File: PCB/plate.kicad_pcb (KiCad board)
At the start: 2 copper layers, 354 x 121 mm, 126 parts, among them SW10 EC_SW, SW11 EC_SW, SW12 EC_SW, SW13 EC_SW, SW14 EC_SW, SW15 EC_SW, SW16 EC_SW, SW17 EC_SW, SW18 EC_SW, SW19 EC_SW, SW2 EC_SW, SW20 EC_SW, SW21 EC_SW, SW22 EC_SW, SW23 EC_SW, SW24 EC_SW, SW25 EC_SW, SW26 EC_SW, SW27 EC_SW, SW28 EC_SW, SW29 EC_SW, SW3 EC_SW, SW30 EC_SW, SW31 EC_SW, SW32 EC_SW, SW33 EC_SW, SW34 EC_SW, SW35 EC_SW, SW36 EC_SW, SW37 EC_SW, SW38 EC_SW, SW39 EC_SW, SW4 EC_SW, SW40 EC_SW, SW41 EC_SW, SW42 EC_SW, SW43 EC_SW, SW44 EC_SW, SW45 EC_SW, SW46 EC_SW, SW47 EC_SW, SW48 EC_SW, SW49 EC_SW, SW5 EC_SW, SW50 EC_SW, SW51 EC_SW, SW52 EC_SW, SW53 EC_SW, SW54 EC_SW, SW55 EC_SW, SW56 EC_SW, SW57 EC_SW, SW58 EC_SW, SW59 EC_SW, SW6 EC_SW, SW60 EC_SW, SW61 EC_SW, SW62 EC_SW, SW63 EC_SW, SW64 EC_SW, SW65 EC_SW, SW66 EC_SW, SW67 EC_SW, SW68 EC_SW, SW69 EC_SW, SW7 EC_SW, SW70 EC_SW, SW71 EC_SW, SW72 EC_SW, SW73 EC_SW, SW74 EC_SW, SW75 EC_SW, SW76 EC_SW, SW77 EC_SW, SW78 EC_SW, SW79 EC_SW, SW8 EC_SW, SW80 EC_SW, SW81 EC_SW, SW82 EC_SW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

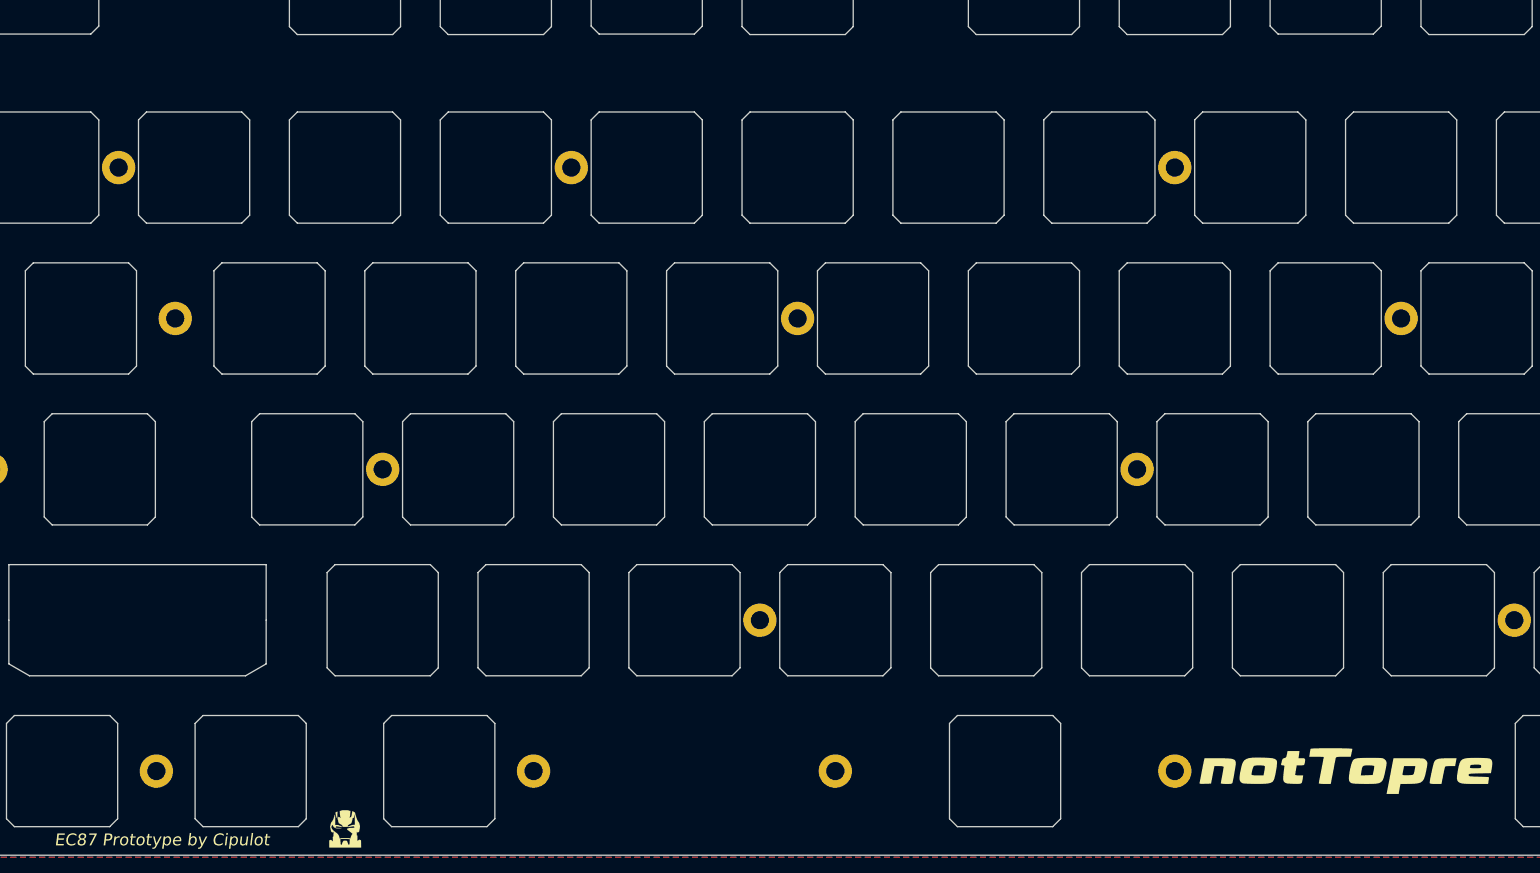
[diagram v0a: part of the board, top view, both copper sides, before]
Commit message: Added stabs cutouts
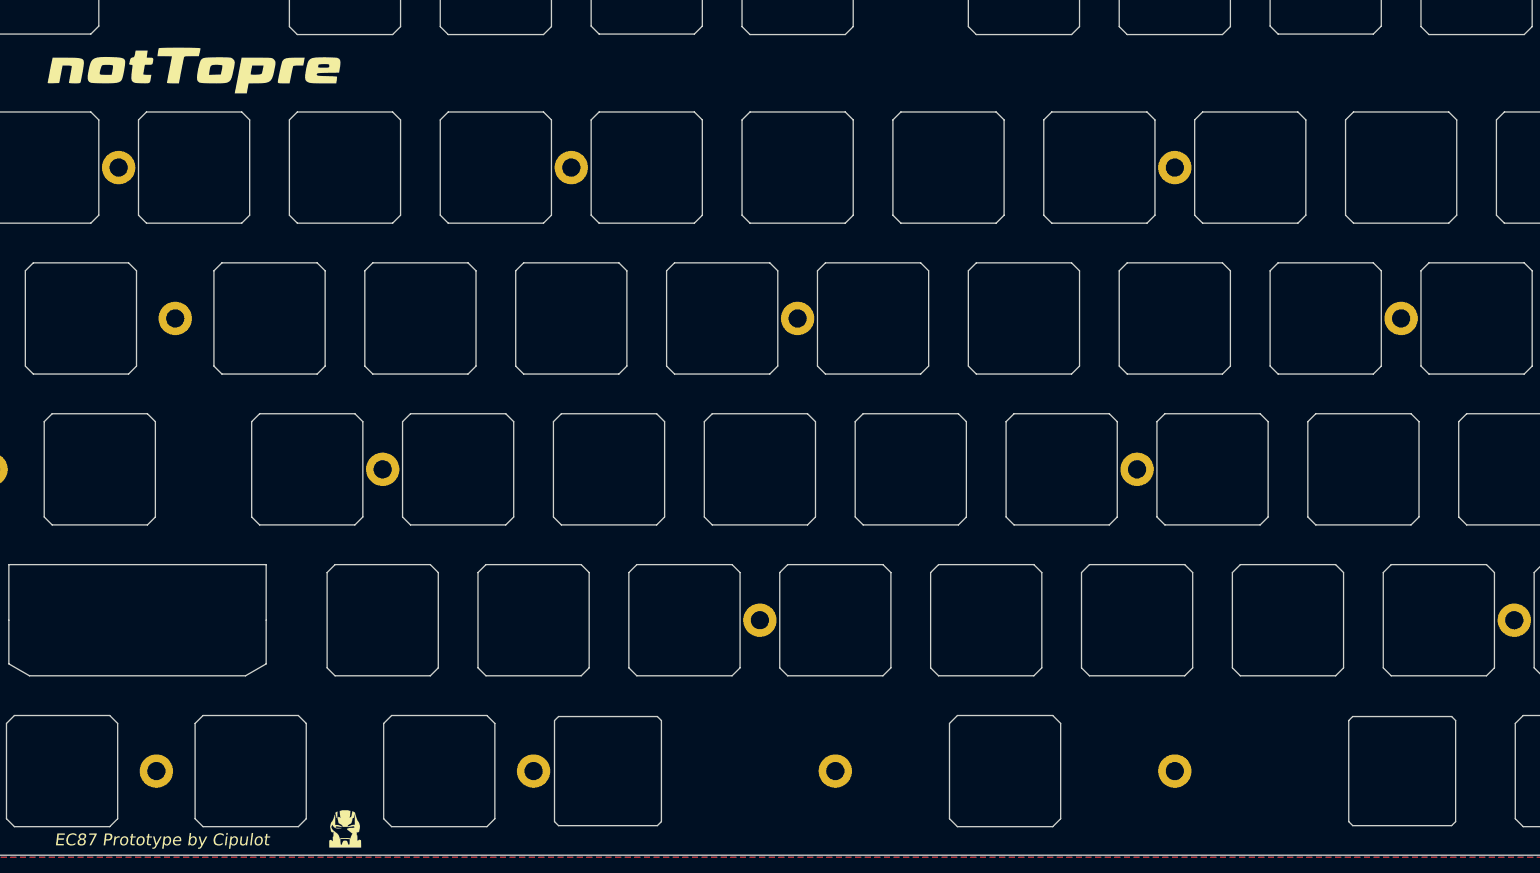
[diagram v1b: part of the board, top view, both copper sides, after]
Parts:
- added REF**: Value, cipulot_parts:plate_cut_space_stab_ecs_pad, F.Cu at (170.0, 193.6)
- moved G*** 169.8 mm to (67.8, 105.3)
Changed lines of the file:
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@@
   )
   (footprint "LOGO" (layer "F.Cu")
-    (at 212.88 193.55)
+    (at 67.83 105.33)
     (attr board_only exclude_from_pos_files exclude_from_bom)
     (fp_text reference "G***" (at 0 0) (layer "F.SilkS") hide
@@
     (model "${KICAD6_3DMODEL_DIR}/cipulot_parts.3dshapes/Topre_Housing.step"
       (offset (xyz -9.3 -9.05 0.65))
+      (scale (xyz 1 1 1))
+      (rotate (xyz 0 0 0))
+    )
+  )
+  (footprint "cipulot_parts:plate_cut_space_stab_ecs_pad" (layer "F.Cu")
+    (at 169.955 193.55)
+    (descr " StepUp generated footprint")
+    (attr smd)
+    (fp_text reference "REF**" (at -45.2628 -8.4328) (layer "Dwgs.User")
+      (effects (font (size 0.8 0.8) (thickness 0.12)))
+    )
+    (fp_text value "Value " (at -4.9 -5.6) (layer "F.SilkS") hide
+      (effects (font (size 0.8 0.8) (thickness 0.12)))
+    )
+    (fp_line (start -43.2755 -6.3635) (end -43.7825 -6.8705) (layer "Edge.Cuts") (width 0.12))
+    (fp_line (start 43.2755 -6.3635) (end 43.7755 -6.8705) (layer "Edge.Cuts") (width 0.12))
+    (fp_line (start -43.7825 -6.8705) (end -56.2305 -6.8705) (layer "Edge.Cuts") (width 0.12))
+    (fp_line (start -56.7375 -6.3635) (end -56.7375 6.3635) (layer "Edge.Cuts") (width 0.12))
+    (fp_line (start -43.7825 6.8705) (end -43.2755 6.3635) (layer "Edge.Cuts") (width 0.12))
+    (fp_line (start 43.7755 -6.8705) (end 56.2375 -6.8705) (layer "Edge.Cuts") (width 0.12))
+    (fp_line (start 43.7825 6.8705) (end 56.2305 6.8705) (layer "Edge.Cuts") (width 0.12))
+    (fp_line (start 56.2375 -6.8705) (end 56.7375 -6.3635) (layer "Edge.Cuts") (width 0.12))
+    (fp_line (start 43.2755 6.3635) (end 43.7825 6.8705) (layer "Edge.Cuts") (width 0.12))
+    (fp_line (start -56.2305 6.8705) (end -43.7825 6.8705) (layer "Edge.Cuts") (width 0.12))
+    (fp_line (start -56.2305 -6.8705) (end -56.7375 -6.3635) (layer "Edge.Cuts") (width 0.12))
+    (fp_line (start 43.2755 -6.3635) (end 43.2755 6.3635) (layer "Edge.Cuts") (width 0.12))
+    (fp_line (start -56.7375 6.3635) (end -56.2305 6.8705) (layer "Edge.Cuts") (width 0.12))
+    (fp_line (start 56.2305 6.8705) (end 56.7375 6.3635) (layer "Edge.Cuts") (width 0.12))
+    (fp_line (start 56.7375 6.3635) (end 56.7375 -6.3635) (layer "Edge.Cuts") (width 0.12))
+    (fp_line (start -43.2755 6.3635) (end -43.2755 -6.3635) (layer "Edge.Cuts") (width 0.12))
+    (model "${KICAD6_3DMODEL_DIR}/cipulot_parts.3dshapes/Topre_Housing.step"
+      (offset (xyz -9.3 -9.05 0.65))
